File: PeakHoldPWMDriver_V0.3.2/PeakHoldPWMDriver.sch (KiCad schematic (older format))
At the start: 121 parts, among them J1 RND 205-00203, J2 RND 205-00205, Q1 2N7002, Q10 2N7002, Q11 2N7002, Q12 2N7002, Q13 TSM2309, Q14 IRLL 024N, Q15 TSM2309, Q16 IRLL 024N, Q17 TSM2309, Q18 TSM2309, Q19 TSM2309, Q2 2N7002, Q20 TSM2309, Q3 2N7002, Q4 2N7002, Q5 TSM2309, Q6 TSM2309, Q7 IRLL 024N, Q8 IRLL 024N, Q9 2N7002, U1 74HC32, U2 LM2901, U3 74HC74, U4 LTC6992, U5 74HC74, U6 LM340, U7 74HC08, U8 74HC08

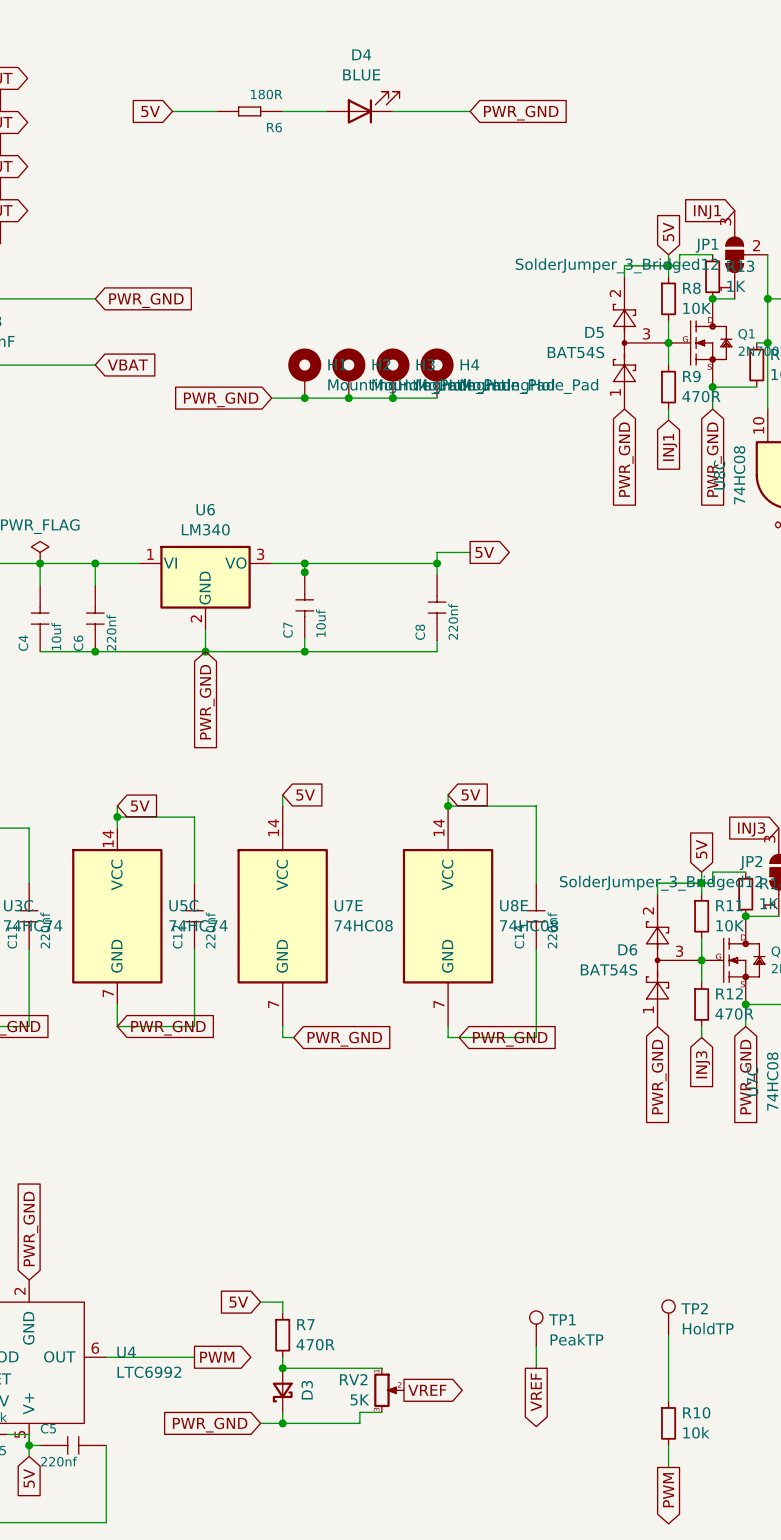
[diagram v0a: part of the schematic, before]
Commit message: Added position csv and BOM files in JLCPCB placement list format
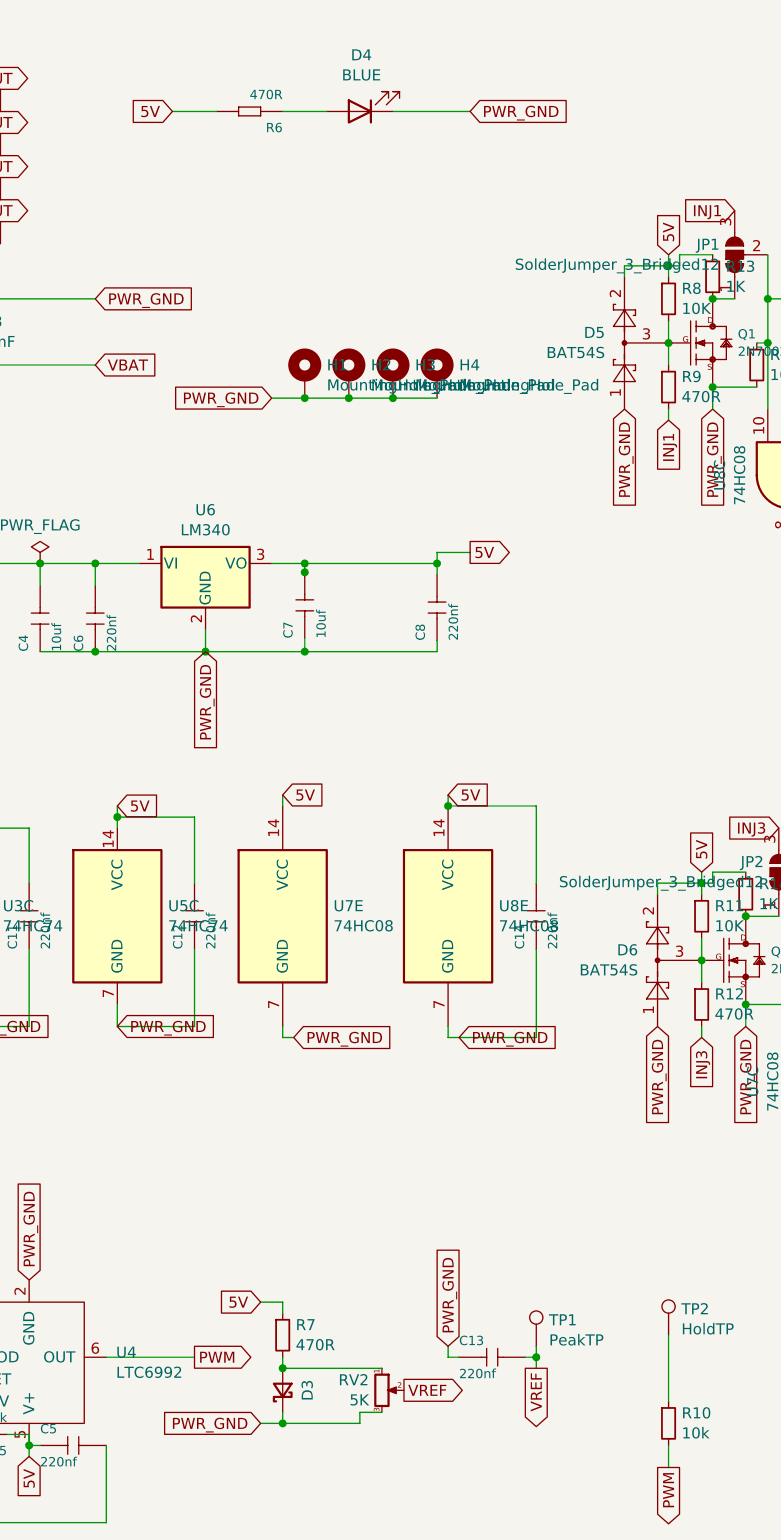
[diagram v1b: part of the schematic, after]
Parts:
- added C13: 220nf, Capacitor_SMD:C_0603_1608Metric_Pad1.05x0.95mm_HandSolder, symbol Speeduino_base-eagle-import:CERAMIC-220NF-25V-10%-X7R(0603)
- C1, C2, C3: LCSC Part # C249474 (none) -> C249474
- C10, C11, C12, C14, C5, C6, C8, C9: LCSC (none) -> C21120
- C4, C7: LCSC (none) -> C13585
- D11: LCSC (none) -> C35722
- D13, D14, D5, D6: LCSC (none) -> C19726
- D3: value BAV103 -> LL4148; LCSC (none) -> C9808
- D4: LCSC (none) -> C375446
- F2: LCSC Part (none) -> C70115
- Q1, Q3: LCSC (none) -> C8545
- Q17, Q5: LCSC (none) -> C15127
- Q7: LCSC (none) -> C189606
- R10, R41, R8: LCSC (none) -> C25804
- R13, R23: LCSC (none) -> C21190
- R15, R17, R7, R9: LCSC (none) -> C23179
- R18: LCSC (none) -> C22775
- R21: LCSC (none) -> C76254
- R3: Field4 (none) -> C23178
- R4: LCSC (none) -> C25803
- R45: LCSC (none) -> C25808
- R47: Field4 (none) -> C4216
- R5: LCSC (none) -> C22809
- R6: value 180R -> 470R; LCSC (none) -> C23179
- U1: LCSC (none) -> C5632
- U2: LCSC (none) -> C163545
- U3, U5: LCSC (none) -> C7345
- U4: LCSC Part # C117381 (none) -> C117381
- U6: LCSC Part # C131990 (none) -> C131990
- U7, U8: LCSC (none) -> C5593
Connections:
- net PWR_GND: now also C13.1
- net VREF: now also C13.2
